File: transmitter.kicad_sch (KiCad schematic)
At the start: 0 parts

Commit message: added schematics and pcb, configure project
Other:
- note added: "MCU - IO"
- note added: "MCU - Power"
- note added: "Transmitter - 2.4GHz"
- note removed: "Power - Sequencing"
- note removed: "Random Sheet 1"
- note removed: "Random Sheet 2"
- title: Cover Page -> Main
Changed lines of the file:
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@@
 	(paper "A3")
 	(title_block
-		(title "Cover Page")
+		(title "Main")
 		(date "Last Modified Date")
 		(rev "${REVISION}")
@@
 		)
 	)
-	(text "Random Sheet 1"
+	(text "MCU - Power"
 		(exclude_from_sim no)
 		(at 45.72 106.68 0)
@@
 		)
 	)
-	(text "Random Sheet 2"
+	(text "MCU - IO"
 		(exclude_from_sim no)
 		(at 45.72 114.3 0)
@@
 		)
 	)
-	(text "Power - Sequencing"
+	(text "Transmitter - 2.4GHz"
 		(exclude_from_sim no)
 		(at 45.72 121.92 0)
@@
 			(project "transmitter"
 				(path "/0650c7a8-acba-429c-9f8e-eec0baf0bc1c"
-					(page "7")
+					(page "3")
 				)
 			)
@@
 			(project "transmitter"
 				(path "/0650c7a8-acba-429c-9f8e-eec0baf0bc1c"
-					(page "3")
+					(page "4")
 				)
 			)
@@
 	)
 	(embedded_fonts no)
+	(embedded_files
+		(file
+			(name "KDT_Template.kicad_wks")
+			(type worksheet)
+			(data |KLUv/WARG30fAPbibSHw1DxoQdkhu4SlLM7X87jHgvDoW2biSU7QYzvgGSgzOQ1hAGAAYwD0Owd7
+				Wf2kqMckqKvvIebk7n1nPrtzNplXk9bXecNBEtM1eJy3WvQ5XcwirPNYzWvVx6Vc9hHu1X9AHZfV
+				PyAw+e5ZxJjx83x3kGONN9XPgqX29c4lx6HqS48II4Jh9lQBlp2UBsntvQh3X2Iyf9TjENRYSqlF
+				eIJ1EpgGnHMSx13j8Ema3EtQ59qvGsnep5lMhtZ5Vd/11tS/9sv9oSr1fYR7pl96Xfv02ieNeKhz
+				9dN+B/FnihpXPznWfId9fPoBmI0ymXD16r6HuLO55Lo6qDAY6rUI9dRFuAlX2bx60DuXOYS9y2bW
+				Vnthlp68TaJJKkZ4rF7MyjT7XjupEcxcs/RatL6hYDhQYv6OMWdCfdeYJOesn9n69OnzPe6wenHc
+				mZ83gMC0hQJ22fp1G6TcHh/3cTooOTU+TfJtW2OCWRcbe/7wmBcEDKPwtAjCyiqG+RKbI+JdOk0C
+				iSRIGvyQO5Gdvk7jPK2CYVjXYEXk4EbQWjeI1m0PboF1DG6yKfQmlzizbJhFyDgW4dP2aYqA7qgR
+				JjMkIpKUFBQkywFQhMiIVVUdQmAQxkAggkA0gjAIFRkBEUgjMERABE0wAgoqyvOE9IyuIAgaMWpl
+				NiWRUpR8oMDgg5aeR6zZDVzhlT7vYn8sWOLQfBJU/iQCW1XovolHGblzFRuXhMrK51dzkXU/+p/n
+				V0zz9rYuG0PTge/eeD5vJflIY8MmThMqPYfAEh2ejGZz75fUFyUG1NnIgiFs4HgbYjkngoMvT+Bm
+				Je0gA6oS2pci8BXd9VaabCb2t/AbzIBGk8csgAgcqKSSY5q4NZ0O6FJn1x1d8BFFgPaafiegVuZC
+				DjMR3/KSwUdA2GkEBzW9R/taoYfIyPb3tB9ODCd7/zXkPzM4OKH8sQv2+m80japD9/0uzrVzH3Vs
+				PyLcPRXaF4Cnkb25ZpdtGRbi0YRpzIhJyRB3VwtbbWkykM7SAC8J3C+iL2/DgKPCPRznmcMecvfc
+				8zgXCwIxXXtrxA3vlyOzRjWGozY1fvQs5K739Rm36D9Gz5BEVz5Q0BN3yKAZtgOnlmMMmXyBElVy
+				MN3dEgRMAQ4XMGJTWKxe3buvxa/aGOLsW931twNOG9MQPKVWKq4edH68ZMnicIsylm5T4il5G/He
+				4A8XF8PHz/D/W/WKVCpeE3NqWLDCOKCM2/DbxfeUbT70YDBz6Flclfz/sO0StBNfl/SW84rwqnWE
+				yE6vf1XeCzdAoyohYFmIEFdSdXuqbvKvgRUU4q+FWRTkg6AmVvECpy1PPuRcFTOp|
+			)
+			(checksum "845A56C585800FA79B7FD4E8CDFE3A25")
+		)
+	)
 )

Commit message: added sd card schematic and refactor page numbers and general tab
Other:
- note added: "Interface - RF Transmitter"
- note added: "Interface - USB FS"
- note added: "LCD - Backlight"
- note added: "LCD - Connectors"
- note added: "Memory - EEPROM"
- note added: "Memory - Flash"
- note added: "Memory - SD Card"
- note added: "Memory - SDRAM"
- note added: "Power - Battery"
- note added: "Power - Charging"
- note added: "Power - Generation"
- note added: "UI - Buttons"
- note added: "UI - Joysticks"
- note added: "UI - LEDs"
- note added: "UI - Rotary encoders"
- note added: "UI - Toggle switches"
- note removed: "Transmitter - 2.4GHz"
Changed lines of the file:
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@@
 		)
 	)
-	(text "..........................................."
+	(text "Memory - EEPROM"
 		(exclude_from_sim no)
 		(at 45.72 152.4 0)
@@
 		)
 	)
-	(text "..........................................."
+	(text "MCU - IO"
 		(exclude_from_sim no)
 		(at 45.72 144.78 0)
@@
 		)
 	)
-	(text "..........................................."
+	(text "MCU - Power"
 		(exclude_from_sim no)
 		(at 45.72 137.16 0)
@@
 		)
 	)
-	(text "..........................................."
+	(text "LCD - Backlight"
 		(exclude_from_sim no)
 		(at 144.78 121.92 0)
@@
 		)
 	)
-	(text "..........................................."
+	(text "Memory - SD Card"
 		(exclude_from_sim no)
 		(at 144.78 99.06 0)
@@
 		)
 	)
-	(text "MCU - Power"
+	(text "Project Architecture"
 		(exclude_from_sim no)
 		(at 45.72 106.68 0)
@@
 		)
 	)
-	(text "..........................................."
+	(text "UI - LEDs"
 		(exclude_from_sim no)
 		(at 243.84 91.44 0)
@@
 		)
 	)
-	(text "MCU - IO"
+	(text "Power - Battery"
 		(exclude_from_sim no)
 		(at 45.72 114.3 0)
@@
 		)
 	)
-	(text "..........................................."
+	(text "UI - Buttons"
 		(exclude_from_sim no)
 		(at 144.78 144.78 0)
@@
 		)
 	)
-	(text "..........................................."
+	(text "Memory - Flash"
 		(exclude_from_sim no)
 		(at 144.78 83.82 0)
@@
 		)
 	)
-	(text "..........................................."
+	(text "LCD - Connectors"
 		(exclude_from_sim no)
 		(at 144.78 129.54 0)
@@
 		)
 	)
-	(text "..........................................."
+	(text "Interface - RF Transmitter"
 		(exclude_from_sim no)
 		(at 144.78 114.3 0)
@@
 		)
 	)
-	(text "..........................................."
+	(text "Interface - USB FS"
 		(exclude_from_sim no)
 		(at 144.78 106.68 0)
@@
 		)
 	)
-	(text "Transmitter - 2.4GHz"
+	(text "Power - Charging"
 		(exclude_from_sim no)
 		(at 45.72 121.92 0)
@@
 		)
 	)
-	(text "..........................................."
+	(text "UI - Joysticks"
 		(exclude_from_sim no)
 		(at 144.78 137.16 0)
@@
 		)
 	)
-	(text "..........................................."
+	(text "UI - Toggle switches"
 		(exclude_from_sim no)
 		(at 144.78 152.4 0)
@@
 		)
 	)
-	(text "..........................................."
+	(text "Memory - SDRAM"
 		(exclude_from_sim no)
 		(at 144.78 91.44 0)
@@
 		)
 	)
-	(text "Project Architecture"
+	(text "Revision History"
 		(exclude_from_sim no)
 		(at 45.72 99.06 0)
@@
 		)
 	)
-	(text "..........................................."
+	(text "UI - Rotary encoders"
 		(exclude_from_sim no)
 		(at 243.84 83.82 0)
@@
 		)
 	)
-	(text "Revision History"
+	(text "Power - Generation"
 		(exclude_from_sim no)
 		(at 45.72 129.54 0)

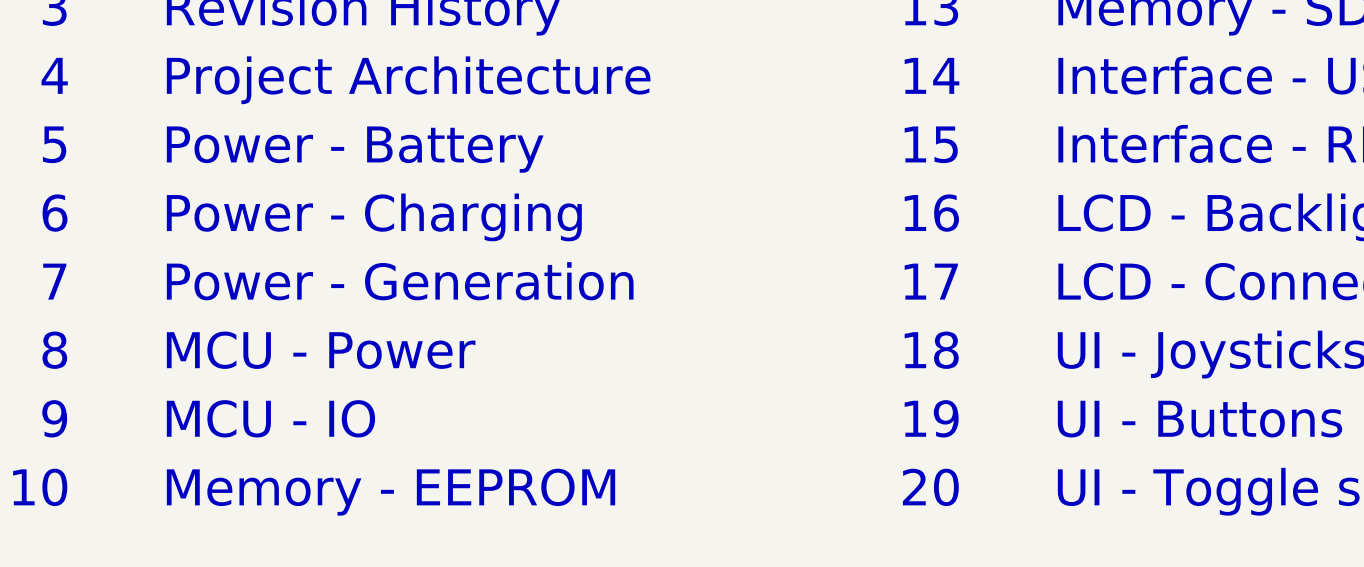
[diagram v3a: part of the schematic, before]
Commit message: added power switch, 5V and 3V3 power generation
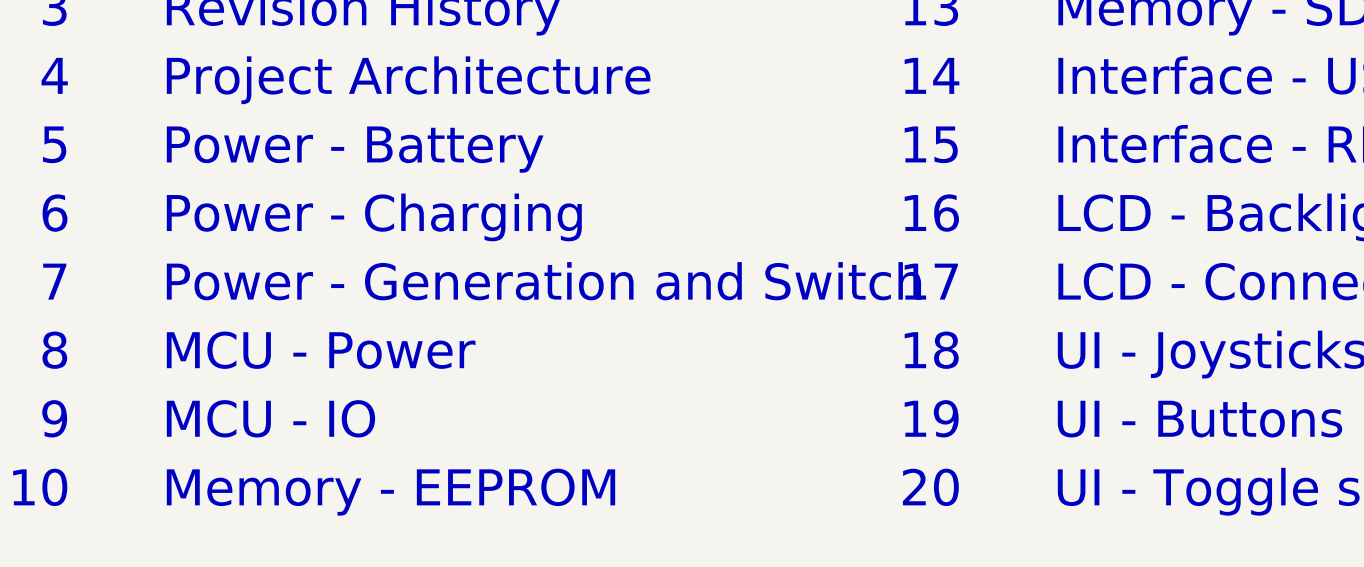
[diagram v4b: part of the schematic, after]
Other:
- note added: "Power - Generation and Switch"
- note removed: "Power - Generation"
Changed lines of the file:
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@@
 		)
 	)
-	(text "Power - Generation"
+	(text "Power - Generation and Switch"
 		(exclude_from_sim no)
 		(at 45.72 129.54 0)

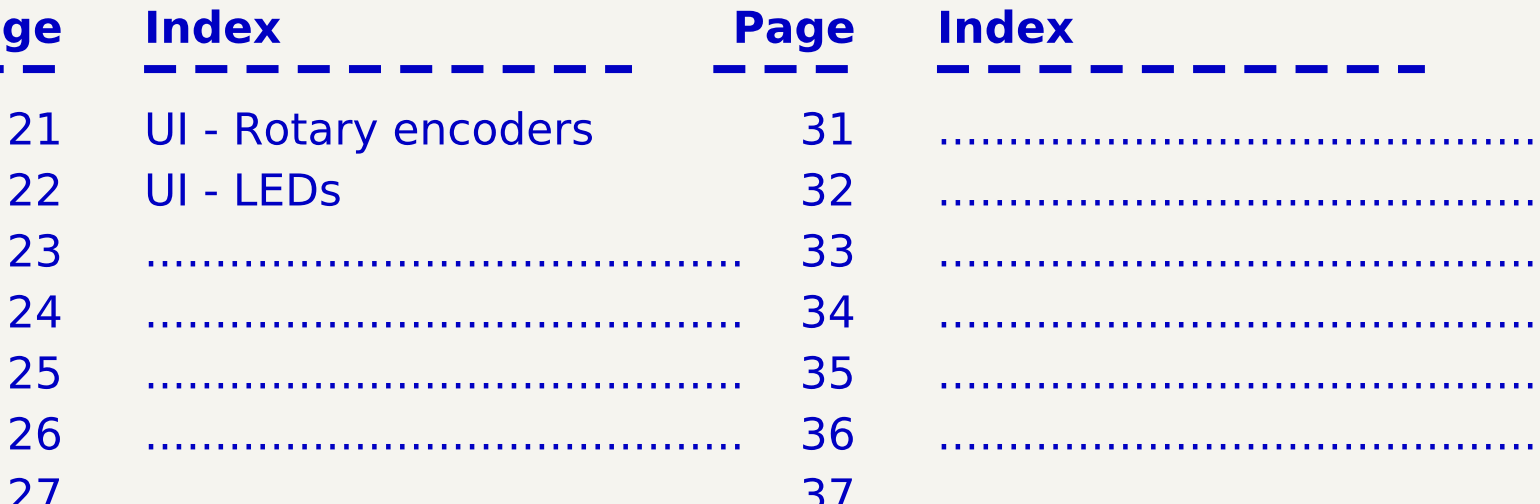
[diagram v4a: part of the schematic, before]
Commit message: added buzzer schematic
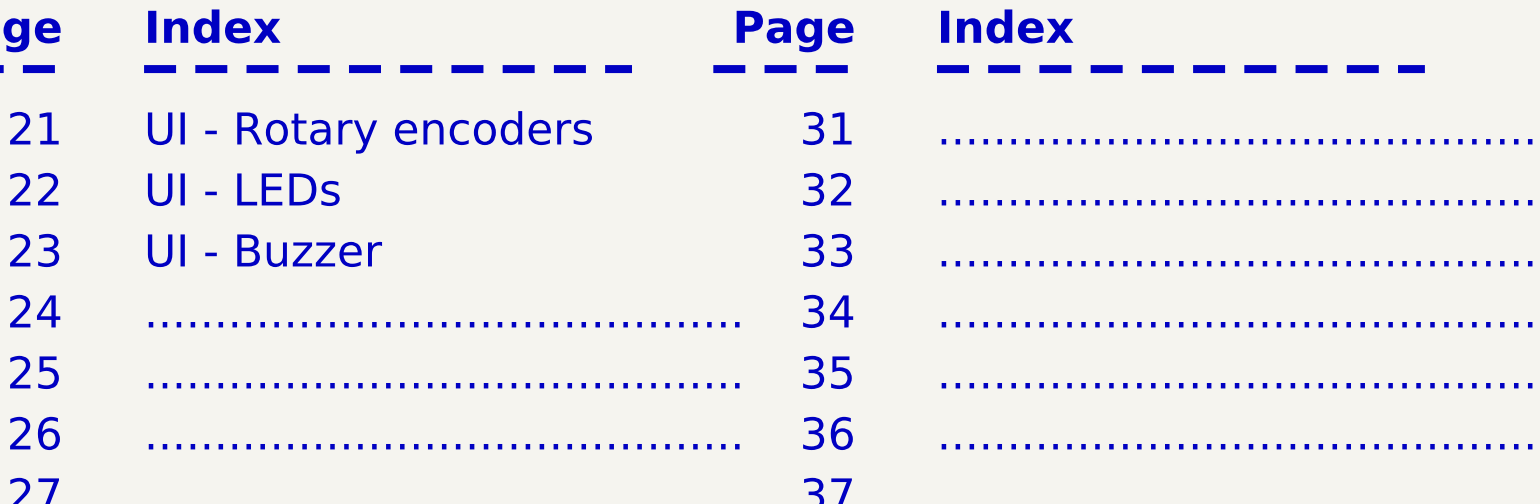
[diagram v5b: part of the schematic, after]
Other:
- note added: "UI - Buzzer"
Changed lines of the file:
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@@
 		)
 	)
-	(text "..........................................."
+	(text "UI - Buzzer"
 		(exclude_from_sim no)
 		(at 243.84 99.06 0)

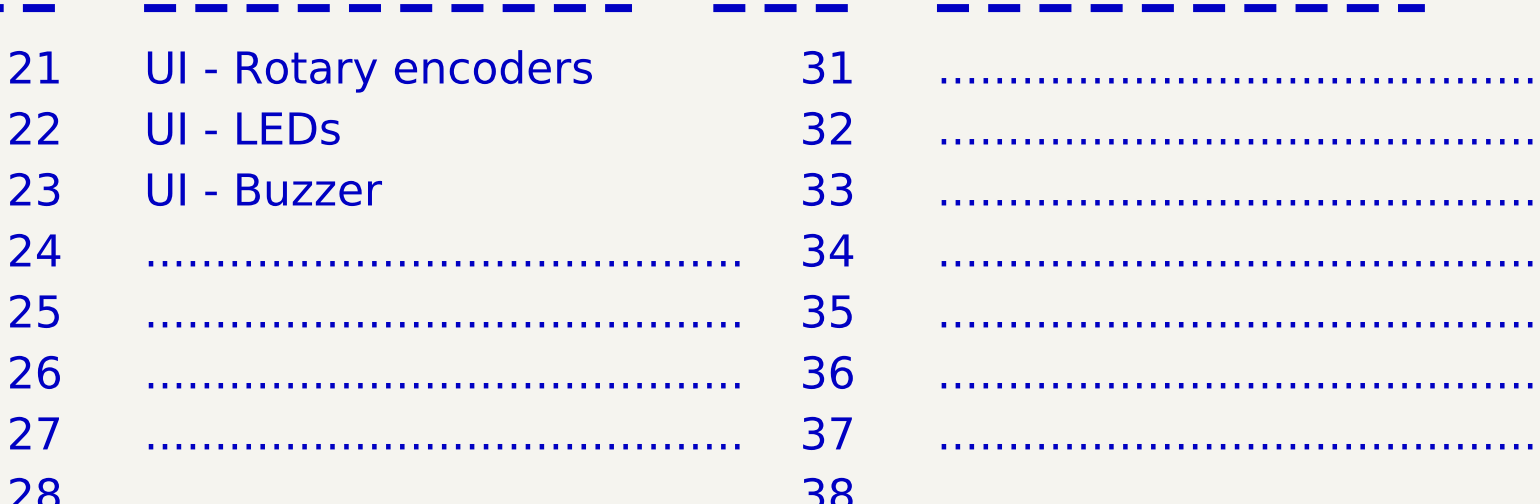
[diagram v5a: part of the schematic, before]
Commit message: added auxiliary schematic, problem with kicad - cannot modify project settings
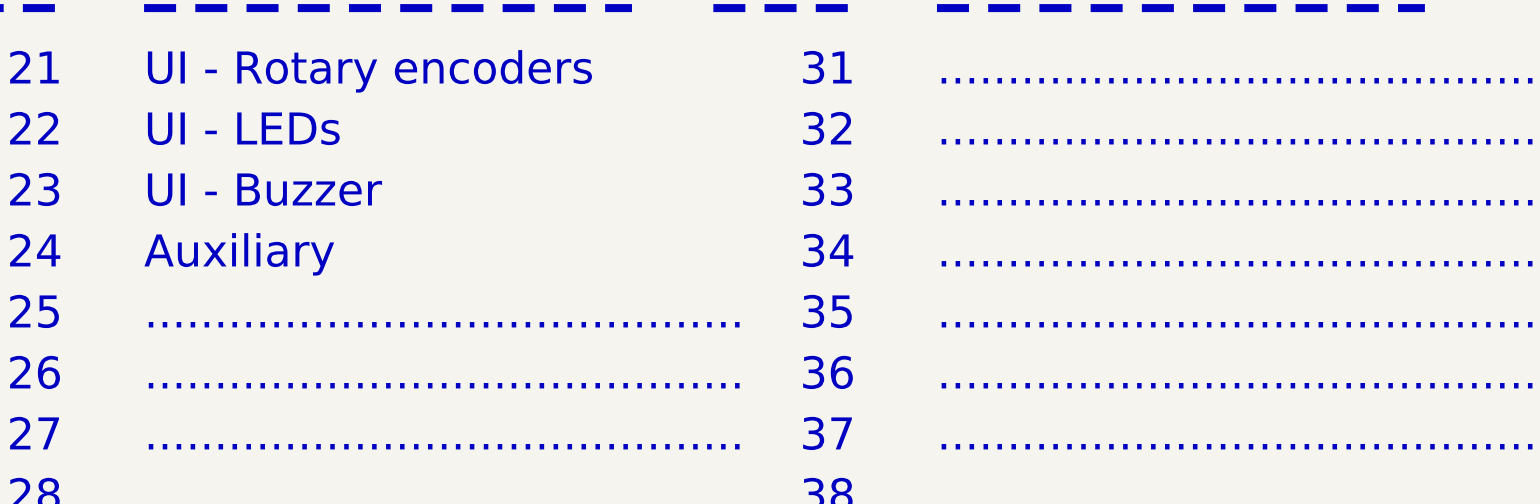
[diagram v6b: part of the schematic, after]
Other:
- note added: "Auxiliary"
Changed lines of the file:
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@@
 		)
 	)
-	(text "..........................................."
+	(text "Auxiliary\n"
 		(exclude_from_sim no)
 		(at 243.84 106.68 0)
